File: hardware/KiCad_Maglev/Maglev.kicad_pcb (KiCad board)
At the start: 4 copper layers, 265 x 130 mm, 110 parts, among them IC1 TLV1117LV33DCYR, J1 USB_C_Receptacle, J11 690367190672, J12 690367190672, J2 691103110002, J3 61300621121, J4 61300821121, J5 61300821121, J6 61300621121, J7 690367191672, J8 690367191672, U1 WE-TVS-82400102, U2 ESP32-C3, U4 TMAG5173A2QDBVRQ1, U5 TPS259474ARPWR, Y1 IQXC-42_830108213209

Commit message: Improved power pcb a little and added silkscreen description
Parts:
- R10, R8, R9: value 1206_R_560112132020 -> 0805_R_560112120030; footprint Resistor_SMD_Wurth:R_Wurth_WRIS-RSKS-1206_R -> Resistor_SMD_Wurth:R_Wurth_WRIS-RSKS-0805_R
- moved R11 61.7 mm to (262.9, 52.5)
- moved R8 33.1 mm to (95.0, 81.8), turned to -135 degrees
- moved R9 31.1 mm to (96.8, 83.4), turned to -135 degrees
- moved R10 29.9 mm to (98.5, 85.0), turned to -135 degrees
- moved C10 0.45 mm to (80.0, 103.0)
- turned HALL to 0 degrees
- renumbered U3 to HALL
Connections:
- R10 pad 1: +3.3V -> /I2C_INT
- R10 pad 2: /I2C_INT -> +3.3V
- R8 pad 1: +3.3V -> /I2C_SCL
- R8 pad 2: /I2C_SCL -> +3.3V
- R9 pad 1: +3.3V -> /I2C_SDA
- R9 pad 2: /I2C_SDA -> +3.3V
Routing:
- net /I2C_SDA: track 161.7 -> 138.5 mm
- net /I2C_SCL: track 165.4 -> 143.9 mm
- net /I2C_INT: track 156.8 -> 138.0 mm
- net /EM_D_P: track 152.8 -> 140.0 mm
- net /EM_D_N: track 147.2 -> 138.2 mm
- net +3.3V: track 71.7 -> 63.7 mm, vias 20 -> 25
- net /EM_C_P: track 176.9 -> 169.6 mm
- net /EM_C_N: track 172.5 -> 165.1 mm
- net GND: track 147.1 -> 141.3 mm, vias 61 -> 199
- added copper zone on B.Cu, net +3.3V
- added copper zone on B.Cu, net GND
- added copper zone on F.Cu, net GND
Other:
- board text added: "COIL POWER CONNECTOR"
- board text added: "GND"
- board text added: "HALL I2C CONNECTOR"
- board text added: "L1"
- board text added: "L2"
- board text added: "L3"
- board text added: "L4"

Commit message: Mistake in H-Bridge schematic - required rerouting
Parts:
- removed 3P3, GND1, GND2: 61300411121, Connector_THT_Wurth:J_Wurth_WR-PHD_61300411121
- removed FAULT1, REST/BOT1, UART1, USB1, XTAL1: 61300211121, Connector_THT_Wurth:J_Wurth_WR-PHD_61300211121
- removed I2C1: 61300311121, Connector_THT_Wurth:J_Wurth_WR-PHD_61300311121
- removed I_SENSE1: 61300511121, Connector_THT_Wurth:J_Wurth_WR-PHD_61300511121
- removed J4, J5: 61300821121, Connector_THT_Wurth:J_Wurth_WR-PHD_61300821121
- removed PWM&DIR1: 61300811121, Connector_THT_Wurth:J_Wurth_WR-PHD_61300811121
- removed R14: 1206_R_560112132041, Resistor_SMD_Wurth:R_Wurth_WRIS-RSKS-1206_R
- removed R15: 0603_R_560112116048, Resistor_SMD_Wurth:R_Wurth_WRIS-RSKS-0603_R
- removed R6, R7: 1206_R_560112132050, Resistor_SMD_Wurth:R_Wurth_WRIS-RSKS-1206_R
- removed Status_LED_RX1, Status_LED_TX1: 0603dome_150060VS86000, LED_SMD_Wurth:D_Wurth_WL-SMCW-0603dome
- added R20: 1206_R_560112132041, Resistor_SMD_Wurth:R_Wurth_WRIS-RSKS-1206_R, B.Cu at (235.0, 68.8)
- added R21: 0603_R_560112116048, Resistor_SMD_Wurth:R_Wurth_WRIS-RSKS-0603_R, B.Cu at (230.2, 68.8)
- added R22: 0805_R_560112120002, Resistor_SMD_Wurth:R_Wurth_WRIS-RSKS-0805_R, B.Cu at (236.2, 65.8)
- added R23: 0805_R_560112120002, Resistor_SMD_Wurth:R_Wurth_WRIS-RSKS-0805_R, B.Cu at (232.2, 65.8)
- added R24: 0805_R_560112120002, Resistor_SMD_Wurth:R_Wurth_WRIS-RSKS-0805_R, B.Cu at (228.2, 65.8)
- added R25: 1206_R_560112132041, Resistor_SMD_Wurth:R_Wurth_WRIS-RSKS-1206_R, B.Cu at (208.0, 68.7)
- added R26: 0603_R_560112116048, Resistor_SMD_Wurth:R_Wurth_WRIS-RSKS-0603_R, B.Cu at (203.2, 68.7)
- added R27: 0805_R_560112120002, Resistor_SMD_Wurth:R_Wurth_WRIS-RSKS-0805_R, B.Cu at (209.2, 65.7)
- added R28: 0805_R_560112120002, Resistor_SMD_Wurth:R_Wurth_WRIS-RSKS-0805_R, B.Cu at (205.2, 65.7)
- added R29: 0805_R_560112120002, Resistor_SMD_Wurth:R_Wurth_WRIS-RSKS-0805_R, B.Cu at (201.2, 65.7)
- added R30: 1206_R_560112132041, Resistor_SMD_Wurth:R_Wurth_WRIS-RSKS-1206_R, B.Cu at (234.8, 84.7)
- added R31: 0603_R_560112116048, Resistor_SMD_Wurth:R_Wurth_WRIS-RSKS-0603_R, B.Cu at (230.0, 84.8)
- added R32: 0805_R_560112120002, Resistor_SMD_Wurth:R_Wurth_WRIS-RSKS-0805_R, B.Cu at (236.0, 81.7)
- added R33: 0805_R_560112120002, Resistor_SMD_Wurth:R_Wurth_WRIS-RSKS-0805_R, B.Cu at (232.0, 81.7)
- added R34: 0805_R_560112120002, Resistor_SMD_Wurth:R_Wurth_WRIS-RSKS-0805_R, B.Cu at (228.0, 81.8)
- added R35: 1206_R_560112132041, Resistor_SMD_Wurth:R_Wurth_WRIS-RSKS-1206_R, B.Cu at (207.8, 84.5)
- added R36: 0603_R_560112116048, Resistor_SMD_Wurth:R_Wurth_WRIS-RSKS-0603_R, B.Cu at (203.0, 84.5)
- added R37: 0805_R_560112120002, Resistor_SMD_Wurth:R_Wurth_WRIS-RSKS-0805_R, B.Cu at (209.0, 81.5)
- added R38: 0805_R_560112120002, Resistor_SMD_Wurth:R_Wurth_WRIS-RSKS-0805_R, B.Cu at (205.0, 81.5)
- added R39: 0805_R_560112120002, Resistor_SMD_Wurth:R_Wurth_WRIS-RSKS-0805_R, B.Cu at (201.0, 81.5)
- C17, C18, C25, C26: value D8L11.5_870585774003 -> 1210_H2.5_885012109011; footprint Capacitor_THT_Wurth:CP_Wurth_WCAP-HTAH-D8L11.5 -> Capacitor_SMD_Wurth:C_Wurth_WCAP-CSGP-1210_H2.5; moved to B.Cu
- J6: moved to F.Cu
- moved J6 129.3 mm to (239.3, 47.8), turned to -112.5 degrees
- moved C12 85.4 mm to (194.7, 60.3), turned to 180 degrees
- moved C16 82.0 mm to (194.6, 65.1)
- moved C14 81.9 mm to (194.7, 62.7), turned to 180 degrees
- moved EMC1 79.5 mm to (203.7, 60.4), turned to 180 degrees
- moved C25 78.9 mm to (194.5, 83.9)
- moved C26 78.5 mm to (194.6, 68.0)
- moved R13 77.2 mm to (211.0, 61.9)
- moved C18 69.6 mm to (221.4, 84.1)
- moved R11 62.5 mm to (213.9, 91.3), turned to 0 degrees
- moved C2 45.8 mm to (185.7, 104.7), turned to 180 degrees
- moved C6 44.7 mm to (185.7, 117.7), turned to 180 degrees
- moved L5 43.5 mm to (181.2, 104.4)
- moved C23 42.0 mm to (221.4, 81.2), turned to 180 degrees
- moved C19 39.4 mm to (221.5, 76.4), turned to 180 degrees
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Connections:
- C17 pad 1: +V_HB -> GND
- C17 pad 2: GND -> +V_HB
- C18 pad 1: +V_HB -> GND
- C18 pad 2: GND -> +V_HB
- C25 pad 1: +V_HB -> GND
- C25 pad 2: GND -> +V_HB
- C26 pad 1: +V_HB -> GND
- C26 pad 2: GND -> +V_HB
- EMA1 pad 4: GND -> /HBRIDG_ALL_FAULT
- EMA1 pad 7: /Electromagnet Driver/IMODE -> Net-(EMA1-IMODE)
- EMB1 pad 4: GND -> /HBRIDG_ALL_FAULT
- EMB1 pad 7: /Electromagnet Driver/IMODE -> Net-(EMB1-IMODE)
- EMC1 pad 4: GND -> /HBRIDG_ALL_FAULT
- EMC1 pad 7: /Electromagnet Driver/IMODE -> Net-(EMC1-IMODE)
- EMD1 pad 4: GND -> /HBRIDG_ALL_FAULT
- EMD1 pad 7: /Electromagnet Driver/IMODE -> Net-(EMD1-IMODE)
- R11 pad 1: +3.3V -> /HBRIDG_ALL_FAULT
- U2 pad 13: GND -> /HBRIDG_ALL_FAULT
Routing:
- net +V_HB: track 425.3 -> 54.1 mm, vias 2 -> 0
- net /HBRIDG_ALL_FAULT: track 0.00 -> 99.0 mm, vias 0 -> 5
- net /Electromagnet Driver/PMODE: track 0.00 -> 95.8 mm, vias 0 -> 2
- net /HBRIDGE_ALL_EN: track 0.00 -> 94.5 mm, vias 0 -> 2
- net /HBRIDGE_A_ISENSE: track 2.23 -> 74.2 mm, vias 0 -> 2
- net /HBRIDGE_A_PWM: track 0.00 -> 67.1 mm, vias 0 -> 2
- net /HBRIDGE_A_DIR: track 0.00 -> 66.4 mm, vias 0 -> 2
- net /EM_C_N: track 165.1 -> 99.6 mm, vias 1 -> 4
- net /CHIP_EN: track 72.2 -> 16.8 mm, vias 1 -> 2
- net /HBRIDGE_B_ISENSE: track 2.40 -> 56.3 mm, vias 0 -> 2
- net /EM_C_P: track 169.6 -> 117.5 mm, vias 1 -> 8
- net /BOOT: track 76.8 -> 26.2 mm
- net /HBRIDGE_C_PWM: track 0.00 -> 47.9 mm, vias 0 -> 2
- net /HBRIDGE_C_DIR: track 0.00 -> 46.5 mm, vias 0 -> 2
- net /HBRIDGE_C_ISENSE: track 33.0 -> 76.8 mm
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- added copper zone on B.Cu, net /EM_A_N
- added copper zone on F.Cu, net /EM_A_N
- added copper zone on B.Cu, net /EM_A_P
- added copper zone on F.Cu, net /EM_A_P
- added copper zone on B.Cu, net /EM_B_N
- added copper zone on F.Cu, net /EM_B_N
- added copper zone on B.Cu, net /EM_B_P
- added copper zone on F.Cu, net /EM_B_P
- added copper zone on B.Cu, net /EM_C_N
- added copper zone on F.Cu, net /EM_C_N
- added copper zone on B.Cu, net /EM_C_P
- added copper zone on F.Cu, net /EM_C_P
- added copper zone on B.Cu, net /EM_D_N
- added copper zone on F.Cu, net /EM_D_N
- added copper zone on B.Cu, net /EM_D_P
- added copper zone on F.Cu, net /EM_D_P
- added copper zone on B.Cu, net /Electromagnet Driver/PMODE

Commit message: Improved Silkscreen and part positioning, includes basic gerber files
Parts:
- removed POWER_LED1: 0603dome_150060VS86000, LED_SMD_Wurth:D_Wurth_WL-SMCW-0603dome
- removed R5: 1206_R_560112132050, Resistor_SMD_Wurth:R_Wurth_WRIS-RSKS-1206_R
- added J4: 61300821121, Connector_THT_Wurth:J_Wurth_WR-PHD_61300821121, F.Cu at (239.6, 156.2)
- added R6: 1206_R_560112132050, Resistor_SMD_Wurth:R_Wurth_WRIS-RSKS-1206_R, B.Cu at (243.6, 154.7)
- added R7: 1206_R_560112132050, Resistor_SMD_Wurth:R_Wurth_WRIS-RSKS-1206_R, B.Cu at (241.0, 148.7)
- added Status_LED_RX1: 0603dome_150060VS86000, LED_SMD_Wurth:D_Wurth_WL-SMCW-0603dome, F.Cu at (243.0, 152.4)
- added Status_LED_TX1: 0603dome_150060VS86000, LED_SMD_Wurth:D_Wurth_WL-SMCW-0603dome, F.Cu at (242.2, 150.5)
- C1: moved to B.Cu
- moved C8 47.9 mm to (221.0, 91.8), turned to 45 degrees
- moved C5 41.4 mm to (219.2, 90.0), turned to 45 degrees
- moved C9 32.9 mm to (209.7, 104.9), turned to 135 degrees
- moved C2 29.3 mm to (214.6, 109.7), turned to -135 degrees
- moved C6 28.8 mm to (212.8, 107.9), turned to -135 degrees
- moved L5 28.0 mm to (209.0, 107.8), turned to 45 degrees
- moved C4 26.8 mm to (208.8, 97.6), turned to 90 degrees
- moved C7 23.4 mm to (205.3, 108.1), turned to 135 degrees
- moved C3 23.3 mm to (208.7, 111.4), turned to -45 degrees
- moved R3 11.2 mm to (163.2, 128.5), turned to 30 degrees
- moved R4 11.0 mm to (186.1, 150.0), turned to 60 degrees
- moved C28 10.7 mm to (256.2, 126.7), turned to 135 degrees
- moved R18 10.4 mm to (255.1, 128.9), turned to 135 degrees
- moved C30 10.3 mm to (252.9, 130.0), turned to 135 degrees
- moved J3 6.93 mm to (273.1, 109.0), turned to 168.75 degrees
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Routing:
- net +V_HB: track 54.1 -> 187.5 mm, vias 0 -> 4
- net /CHIP_EN: track 16.8 -> 68.8 mm
- net /USB_D+: track 0.00 -> 47.1 mm, vias 0 -> 2
- net /BOOT: track 26.2 -> 73.1 mm
- net /USB_D-: track 1.28 -> 48.2 mm, vias 0 -> 2
- net /USB Power Circuit/USB_VBUS: track 38.1 -> 22.4 mm, vias 1 -> 0
- net +5VP: track 56.3 -> 43.1 mm, vias 1 -> 0
- net GND: track 116.5 -> 104.1 mm, vias 345 -> 352
- net /VDD3P3: track 0.00 -> 12.2 mm
- net +5V: track 13.0 -> 2.70 mm
- net (no net): track 9.68 -> 2.71 mm
- net Net-(POWER_LED1-+): track 4.40 -> 0.00 mm, vias 1 -> 0
- net Net-(Status_LED_RX1-+): track 0.00 -> 3.56 mm, vias 0 -> 1
- net Net-(Status_LED_TX1-+): track 0.00 -> 3.51 mm, vias 0 -> 1
- net /HBRIDGE_C_DIR: track 46.5 -> 49.8 mm
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- added copper zone on B.Cu, net +5V
- added copper zone on In2.Cu, net +V_HB
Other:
- board text added: "LED 1"
- board text added: "LED 2"

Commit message: changed usb-c connector because pcbway cant handle the old one, cleared all design rule errors
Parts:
- J1: footprint WURTH_USB:632723300011 -> WURTH_USB:629722000214
- moved R1 5.46 mm to (252.4, 135.0), turned to 135 degrees
- moved J1 3.50 mm to (258.5, 143.5)
- moved Magnet2 0.45 mm to (214.8, 99.6)
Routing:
- net Net-(U2-U0RXD/GPIO20): track 0.00 -> 68.1 mm
- net Net-(U2-U0TXD/GPIO21): track 0.00 -> 62.7 mm
- net /USB Power Circuit/USB_VBUS: track 22.4 -> 46.2 mm, vias 0 -> 4
- net /HBRIDGE_ALL_EN: track 94.5 -> 114.4 mm
- net +3.3V: track 44.9 -> 51.6 mm, vias 36 -> 40
- net Net-(J1-D--PadA7): track 10.7 -> 15.0 mm
- net Net-(J1-D+-PadA6): track 9.73 -> 13.9 mm
- net /HBRIDGE_B_ISENSE: track 57.5 -> 60.9 mm
- net /HBRIDGE_A_ISENSE: track 75.4 -> 78.5 mm
- net /HBRIDGE_C_DIR: track 49.8 -> 46.7 mm
- net /USB_D+: track 47.1 -> 50.3 mm
- net Net-(J1-CC2): track 1.64 -> 4.63 mm, vias 0 -> 1
- net (no net): track 2.71 -> 0.00 mm
- net Net-(J1-CC1): track 5.68 -> 8.34 mm
- net /HBRIDGE_C_PWM: track 50.6 -> 48.4 mm
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
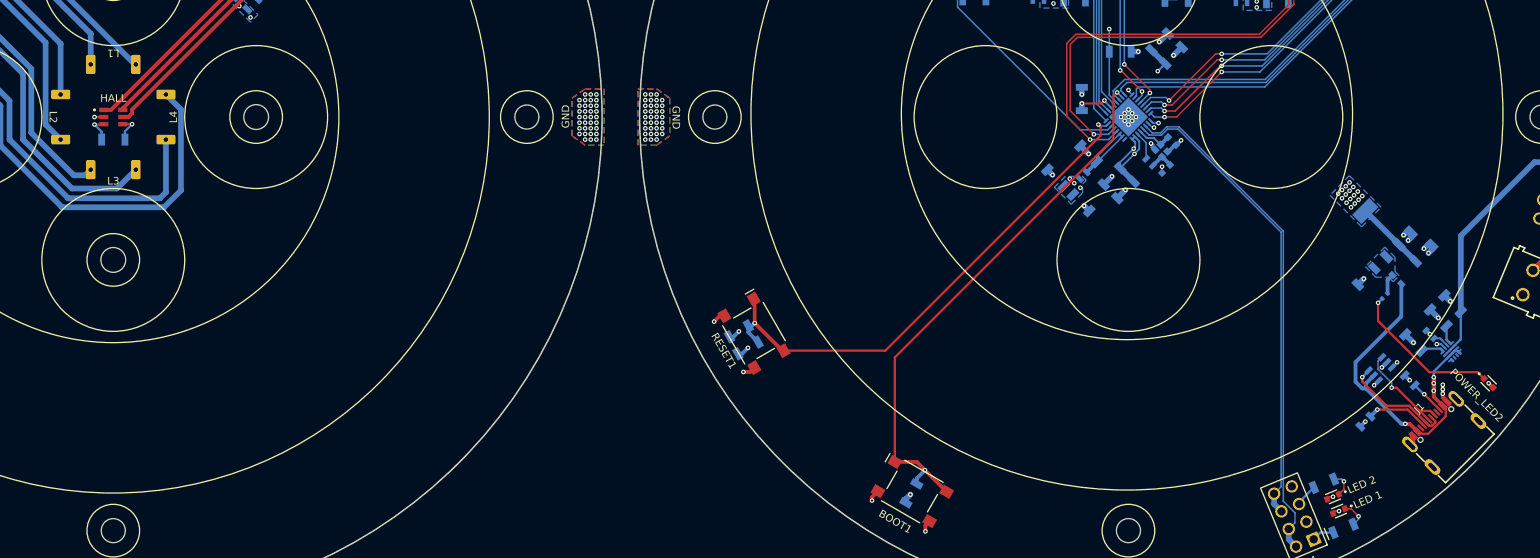
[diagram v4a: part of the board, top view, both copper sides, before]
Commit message: reduced some DRC warnings
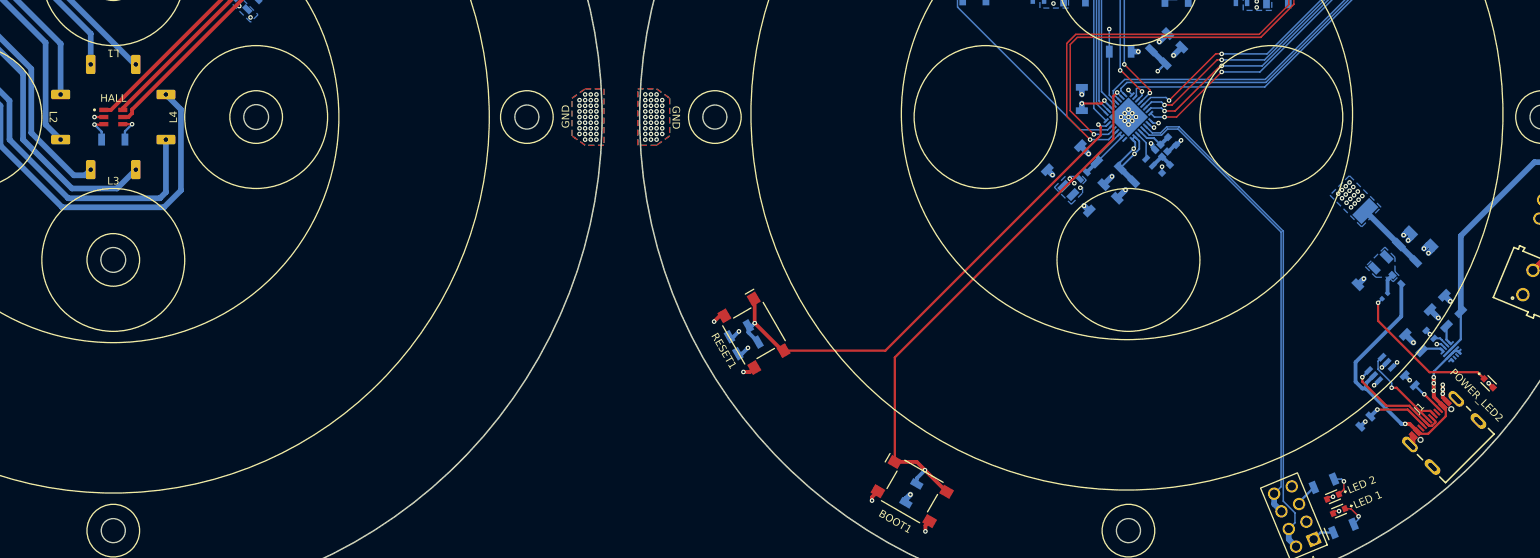
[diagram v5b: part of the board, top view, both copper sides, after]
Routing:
- net +V_HB: track 187.5 -> 189.1 mm
